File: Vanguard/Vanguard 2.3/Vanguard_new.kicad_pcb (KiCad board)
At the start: 4 copper layers, 42.1 x 52.7 mm, 85 parts, among them J1 USB_C_Receptacle_USB2.0_16P, J2 Conn_02x03_Pin, J3 Micro_SD_Card_Det1, J4 STARBOARD_SERVO, J5 PORTSIDE_SERVO, J6 Conn_01x02_Pin, J7 EJECTION_SERVO, Q1 BSS138, Q2 BSS138, Q3 BSS138, Q4 BSS138, U1 ATSAMD11D14A-M, U2 ATmega4809-A, U3 AT25DF641A-SH-T, U4 AP2112K-3.3, U5 BD1020HFV, U6 BNO086, U7 TXB0104D, U8 TPS61092, U9 MPM3610AGQV-P, Y1 32.768kHz

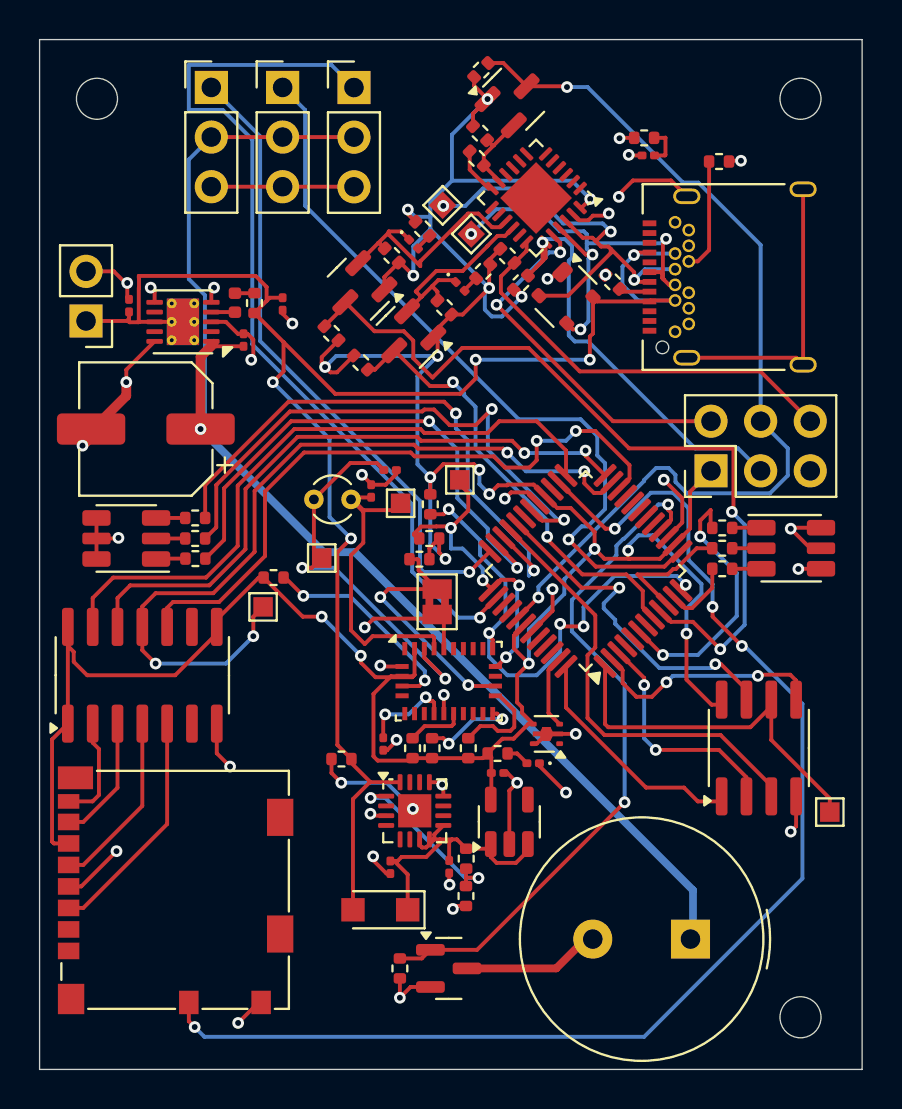
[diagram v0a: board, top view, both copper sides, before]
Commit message: diode added on vbus of usb c
prevents back driving device on usbc line. Led added for power on indication.
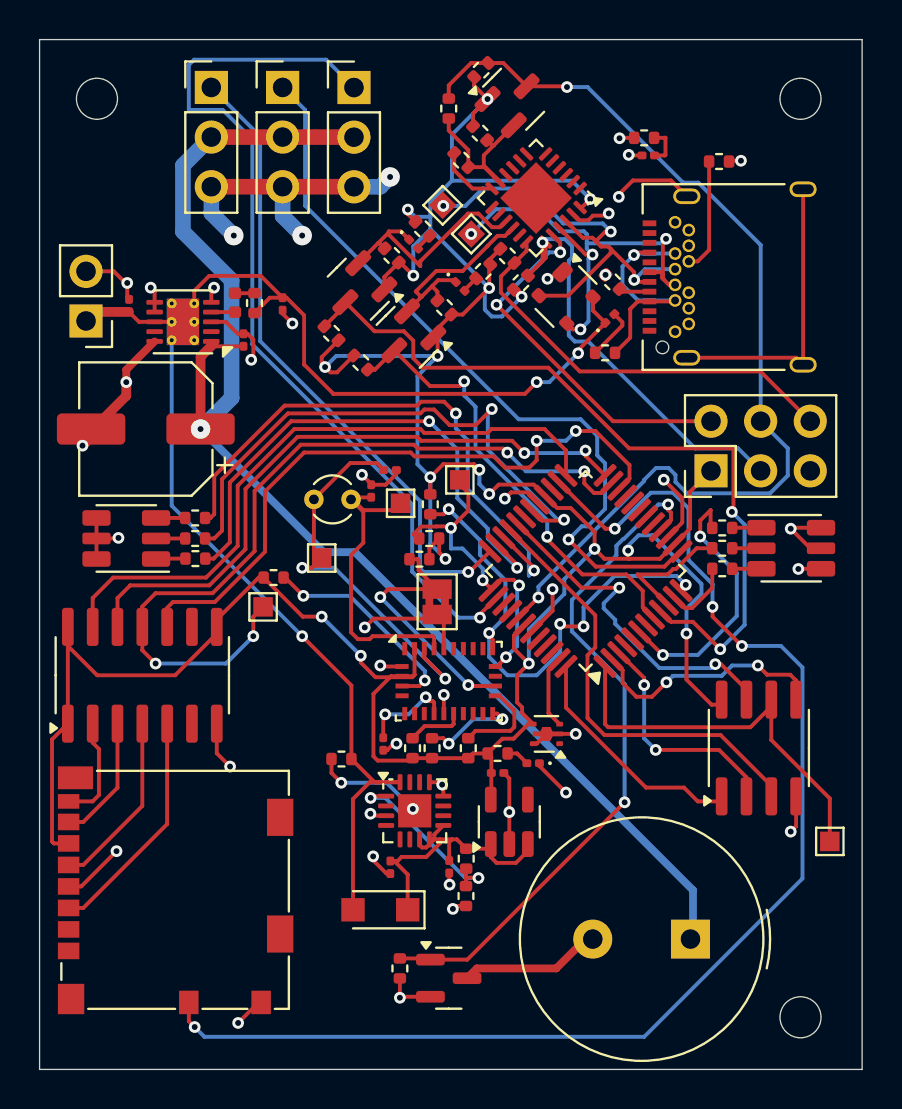
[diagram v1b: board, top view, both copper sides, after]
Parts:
- added D7: LED, LED_SMD:LED_0201_0603Metric, F.Cu at (121.7, 98.2)
- added R35: R220, Resistor_SMD:R_0402_1005Metric, F.Cu at (121.5, 100.0)
- added R8: DNP, Resistor_SMD:R_0402_1005Metric, F.Cu at (113.5, 87.5)
- J6: value Conn_01x02_Pin -> Battery In
- moved TP4 1.50 mm to (133.0, 125.0)
- moved R5 0.80 mm to (114.1, 90.1)
- moved Q4 0.50 mm to (113.5, 132.0)
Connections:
- C4 pad 1: POWER_STAB -> BATT_IN
- C8 pad 1: POWER_STAB -> BATT_IN
- D1 pad 4: POWER_STAB -> BATT_IN
- D6 pad 2: POWER_STAB -> BATT_IN
- J1 pad A4: POWER_STAB -> Net-(J1-VBUS-PadA4)
- J1 pad A9: POWER_STAB -> Net-(J1-VBUS-PadA4)
- J1 pad B4: POWER_STAB -> Net-(J1-VBUS-PadA4)
- J1 pad B9: POWER_STAB -> Net-(J1-VBUS-PadA4)
- J6 pad 1: POWER_STAB -> BATT_IN
- R14 pad 1: POWER_STAB -> BATT_IN
- R33 pad 2: POWER_STAB -> BATT_IN
- U8 pad 11: POWER_STAB -> BATT_IN
- U8 pad 8: POWER_STAB -> BATT_IN
- U9 pad 16: POWER_STAB -> BATT_IN
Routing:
- net POWER_STAB: track 85.7 -> 0.00 mm, vias 5 -> 0
- net BATT_IN: track 0.00 -> 74.5 mm, vias 0 -> 3
- net Net-(J1-VBUS-PadA4): track 0.00 -> 12.8 mm, vias 0 -> 1
- net GND: track 103.6 -> 111.0 mm, vias 38 -> 41
- net /TX_UPDI: track 4.29 -> 9.07 mm
- net UPDI: track 48.7 -> 51.8 mm
- net Net-(D7-A): track 0.00 -> 2.73 mm
- net PA2/SCK: track 19.3 -> 20.8 mm
- net +5V: track 66.6 -> 68.0 mm
- net RX0: track 41.4 -> 40.1 mm
- net CD: track 66.2 -> 67.3 mm
- net /RX_UPDI: track 2.48 -> 3.20 mm
